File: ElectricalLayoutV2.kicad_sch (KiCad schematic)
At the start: 21 parts, among them U1 DS18B20, U2 DS18B20, U3 DS18B20, U4 DS18B20

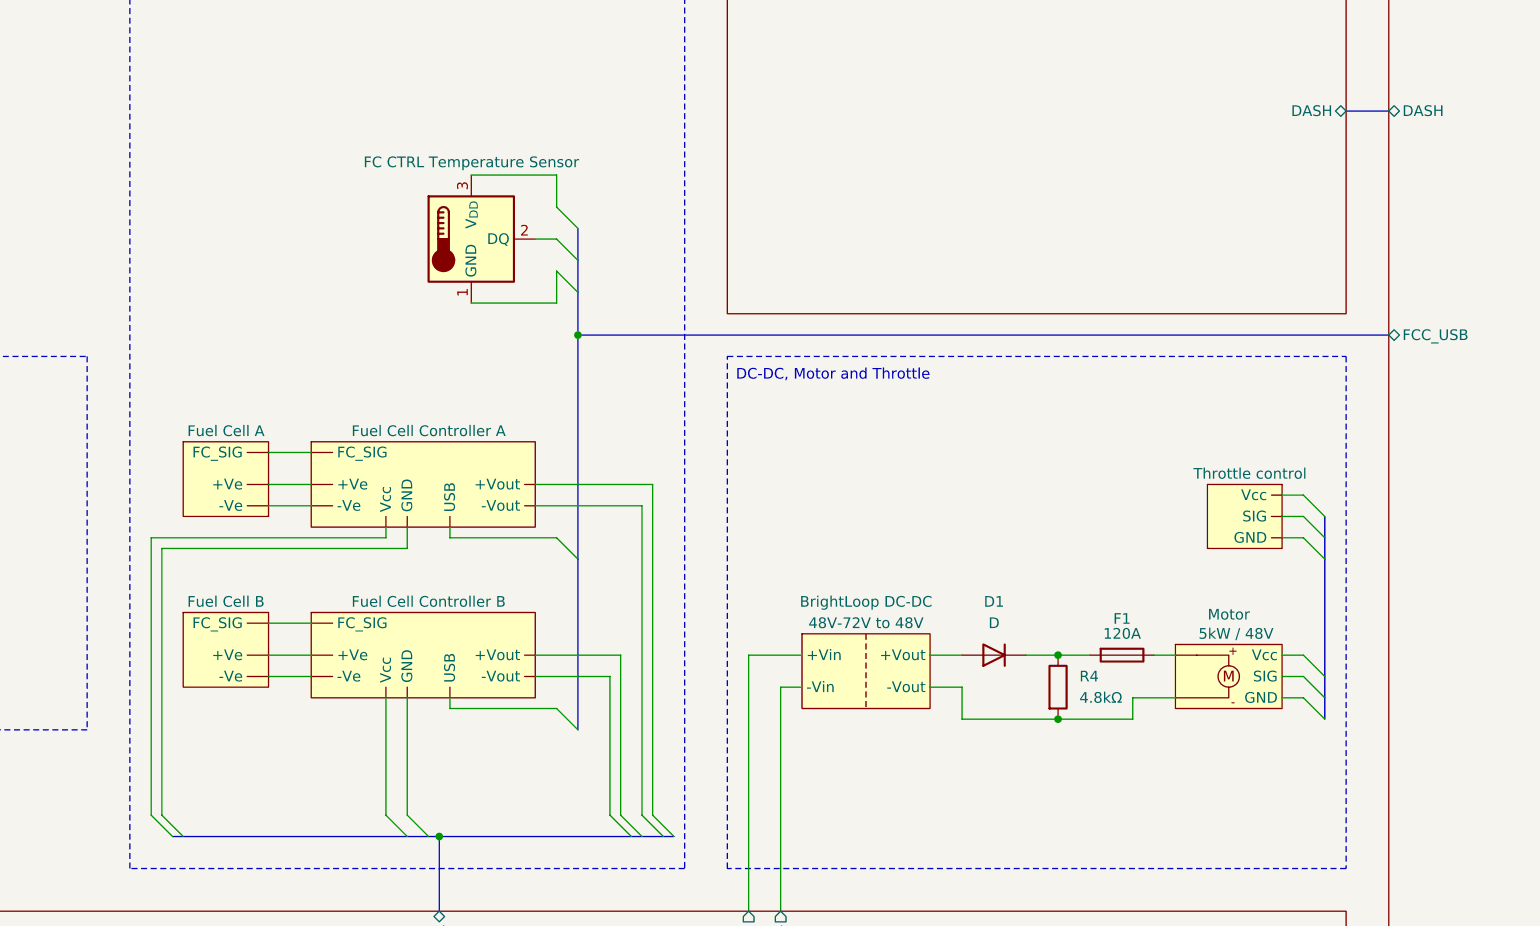
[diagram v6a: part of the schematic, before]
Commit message: Add labels
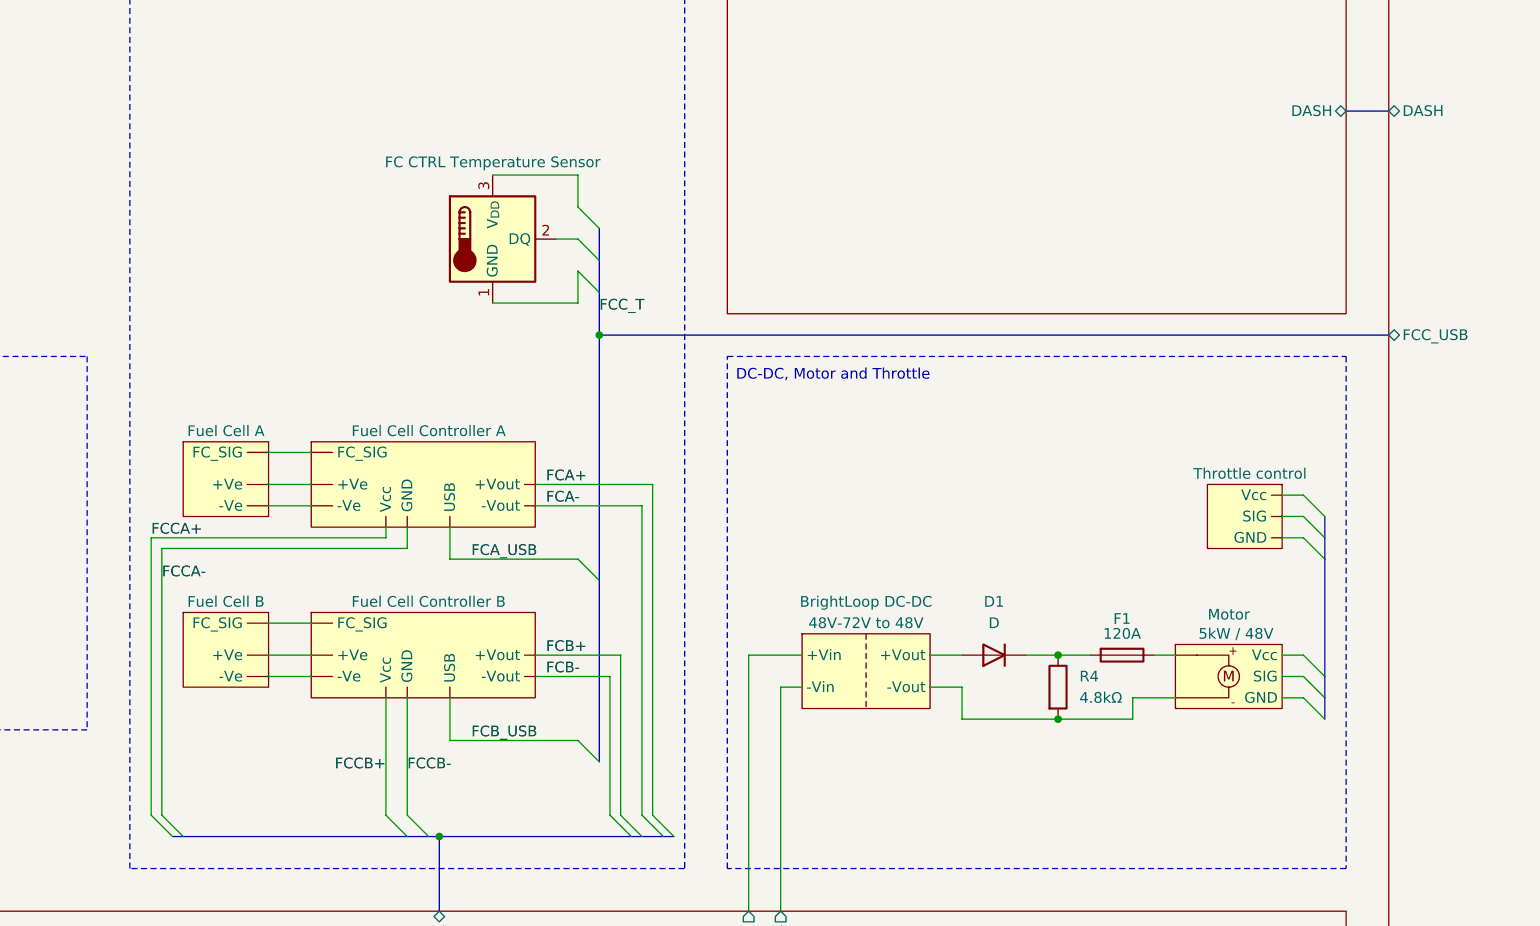
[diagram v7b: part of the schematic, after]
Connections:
- net FCCA-: now reaches FCC1. (Vcc)
- net FCCA-: no longer FC1. (FC_SIG)
- net at PROP1. (Vcc): now also DCC1. (-Vout), R4.2
- net FCCB-: now reaches FCC2. (Vcc)
- new net: FC1. (FC_SIG), FCC1. (Vcc) (x2)
- new net: FC2. (FC_SIG), FCC2. (Vcc) (x2)
- new net FCA+: FCC1. (Vcc)
- new net FCA-: FCC1. (Vcc)
- new net FCA_USB: FCC1. (Vcc)
- new net FCB+: FCC2. (Vcc)
- new net FCB-: FCC2. (Vcc)
- new net FCB_USB: FCC2. (Vcc)
- new net FCCA+: FCC1. (Vcc)
- new net FCCB+: FCC2. (Vcc)
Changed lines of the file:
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@@
 	(title_block
 		(title "Electrical Layout 2024")
-		(date "2024-06-04")
-		(rev "1.3.0")
+		(date "2024-06-13")
+		(rev "1.3.1")
 		(company "Exocet Polytechnique Montréal")
 	)
@@
 	)
 	(junction
+		(at 118.11 60.96)
+		(diameter 0)
+		(color 0 0 132 1)
+	)
+	(junction
 		(at 172.72 99.06)
 		(diameter 0)
@@
 	)
 	(junction
-		(at 115.57 60.96)
-		(diameter 0)
-		(color 0 0 0 0)
-	)
-	(junction
 		(at 172.72 106.68)
 		(diameter 0)
@@
 	)
 	(bus_entry
-		(at 113.03 105.41)
+		(at 115.57 109.22)
 		(size 2.54 2.54)
 		(stroke
@@
 	)
 	(bus_entry
-		(at 113.03 53.34)
+		(at 115.57 53.34)
 		(size 2.54 2.54)
 		(stroke
@@
 	)
 	(bus_entry
-		(at 113.03 45.72)
-		(size 2.54 2.54)
-		(stroke
-			(width 0)
-			(type default)
-		)
-	)
-	(bus_entry
-		(at 113.03 49.53)
+		(at 115.57 45.72)
+		(size 2.54 2.54)
+		(stroke
+			(width 0)
+			(type default)
+		)
+	)
+	(bus_entry
+		(at 115.57 49.53)
 		(size 2.54 2.54)
 		(stroke
@@
 	)
 	(bus_entry
-		(at 113.03 85.09)
+		(at 115.57 87.63)
 		(size 2.54 2.54)
 		(stroke
@@
 	(wire
 		(pts
-			(xy 102.87 41.91) (xy 113.03 41.91)
+			(xy 105.41 41.91) (xy 115.57 41.91)
 		)
 		(stroke
@@
 	(wire
 		(pts
-			(xy 113.03 41.91) (xy 113.03 45.72)
+			(xy 115.57 41.91) (xy 115.57 45.72)
 		)
 		(stroke
@@
 	(wire
 		(pts
-			(xy 100.33 83.82) (xy 100.33 85.09)
+			(xy 100.33 83.82) (xy 100.33 87.63)
 		)
 		(stroke
@@
 	(bus
 		(pts
-			(xy 115.57 87.63) (xy 115.57 107.95)
+			(xy 118.11 90.17) (xy 118.11 111.76)
 		)
 		(stroke
@@
 	(wire
 		(pts
-			(xy 113.03 57.15) (xy 113.03 53.34)
+			(xy 115.57 57.15) (xy 115.57 53.34)
 		)
 		(stroke
@@
 	(bus
 		(pts
-			(xy 115.57 55.88) (xy 115.57 60.96)
-		)
-		(stroke
-			(width 0)
-			(type default)
+			(xy 118.11 55.88) (xy 118.11 60.96)
+		)
+		(stroke
+			(width 0)
+			(type default)
+			(color 132 0 0 1)
 		)
 	)
@@
 	(wire
 		(pts
-			(xy 100.33 105.41) (xy 113.03 105.41)
+			(xy 100.33 109.22) (xy 115.57 109.22)
 		)
 		(stroke
@@
 		)
 	)
-	(bus
-		(pts
-			(xy 115.57 60.96) (xy 212.09 60.96)
-		)
-		(stroke
-			(width 0)
-			(type default)
-		)
-	)
 	(wire
 		(pts
@@
 	(wire
 		(pts
-			(xy 102.87 57.15) (xy 113.03 57.15)
-		)
-		(stroke
-			(width 0)
-			(type default)
-		)
-	)
-	(wire
-		(pts
-			(xy 100.33 85.09) (xy 113.03 85.09)
+			(xy 105.41 57.15) (xy 115.57 57.15)
+		)
+		(stroke
+			(width 0)
+			(type default)
+		)
+	)
+	(wire
+		(pts
+			(xy 100.33 87.63) (xy 115.57 87.63)
 		)
 		(stroke
@@
 	(bus
 		(pts
-			(xy 115.57 87.63) (xy 115.57 60.96)
+			(xy 118.11 90.17) (xy 118.11 60.96)
 		)
 		(stroke
@@
 	(bus
 		(pts
-			(xy 115.57 48.26) (xy 115.57 52.07)
-		)
-		(stroke
-			(width 0)
-			(type default)
+			(xy 118.11 48.26) (xy 118.11 52.07)
+		)
+		(stroke
+			(width 0)
+			(type default)
+			(color 132 0 0 1)
 		)
 	)
@@
 		)
 	)
+	(bus
+		(pts
+			(xy 118.11 60.96) (xy 212.09 60.96)
+		)
+		(stroke
+			(width 0)
+			(type default)
+		)
+	)
 	(wire
 		(pts
@@
 	(wire
 		(pts
-			(xy 110.49 49.53) (xy 113.03 49.53)
+			(xy 113.03 49.53) (xy 115.57 49.53)
 		)
 		(stroke
@@
 	(bus
 		(pts
-			(xy 115.57 52.07) (xy 115.57 55.88)
-		)
-		(stroke
-			(width 0)
-			(type default)
+			(xy 118.11 52.07) (xy 118.11 55.88)
+		)
+		(stroke
+			(width 0)
+			(type default)
+			(color 132 0 0 1)
 		)
 	)
@@
 	(wire
 		(pts
-			(xy 100.33 105.41) (xy 100.33 104.14)
+			(xy 100.33 109.22) (xy 100.33 104.14)
 		)
 		(stroke
@@
 				(size 1.27 1.27)
 				(color 0 0 194 1)
+			)
+			(justify left bottom)
+		)
+	)
+	(label "FCB-"
+		(at 111.76 101.6 0)
+		(fields_autoplaced yes)
+		(effects
+			(font
+				(size 1.27 1.27)
+			)
+			(justify left bottom)
+		)
+	)
+	(label "FCB+"
+		(at 111.76 99.06 0)
+		(fields_autoplaced yes)
+		(effects
+			(font
+				(size 1.27 1.27)
+			)
+			(justify left bottom)
+		)
+	)
+	(label "FCCB-"
+		(at 95.25 113.03 0)
+		(fields_autoplaced yes)
+		(effects
+			(font
+				(size 1.27 1.27)
+			)
+			(justify left bottom)
+		)
+	)
+	(label "FCCA-"
+		(at 66.04 90.17 0)
+		(fields_autoplaced yes)
+		(effects
+			(font
+				(size 1.27 1.27)
+			)
+			(justify left bottom)
+		)
+	)
+	(label "FCA+"
+		(at 111.76 78.74 0)
+		(fields_autoplaced yes)
+		(effects
+			(font
+				(size 1.27 1.27)
+			)
+			(justify left bottom)
+		)
+	)
+	(label "FCCA+"
+		(at 64.77 85.09 0)
+		(fields_autoplaced yes)
+		(effects
+			(font
+				(size 1.27 1.27)
+			)
+			(justify left bottom)
+		)
+	)
+	(label "FCB_USB"
+		(at 102.87 109.22 0)
+		(fields_autoplaced yes)
+		(effects
+			(font
+				(size 1.27 1.27)
+			)
+			(justify left bottom)
+		)
+	)
+	(label "FCCB+"
+		(at 92.71 113.03 180)
+		(fields_autoplaced yes)
+		(effects
+			(font
+				(size 1.27 1.27)
+			)
+			(justify right bottom)
+		)
+	)
+	(label "FCC_T"
+		(at 118.11 58.42 0)
+		(fields_autoplaced yes)
+		(effects
+			(font
+				(size 1.27 1.27)
+			)
+			(justify left bottom)
+		)
+	)
+	(label "FCA_USB"
+		(at 102.87 87.63 0)
+		(fields_autoplaced yes)
+		(effects
+			(font
+				(size 1.27 1.27)
+			)
+			(justify left bottom)
+		)
+	)
+	(label "FCA-"
+		(at 111.76 81.28 0)
+		(fields_autoplaced yes)
+		(effects
+			(font
+				(size 1.27 1.27)
 			)
 			(justify left bottom)
@@
 	(symbol
 		(lib_id "Sensor_Temperature:DS18B20")
-		(at 102.87 49.53 0)
+		(at 105.41 49.53 0)
 		(unit 1)
 		(exclude_from_sim no)
@@
 		(dnp no)
 		(property "Reference" "U1"
-			(at 96.52 48.2599 0)
+			(at 99.06 48.2599 0)
 			(effects
 				(font
@@
 		)
 		(property "Value" "DS18B20"
-			(at 96.52 50.7999 0)
+			(at 99.06 50.7999 0)
 			(effects
 				(font
@@
 		)
 		(property "Footprint" "Package_TO_SOT_THT:TO-92_Inline"
-			(at 77.47 55.88 0)
+			(at 80.01 55.88 0)
 			(effects
 				(font
@@
 		)
 		(property "Datasheet" "http://datasheets.maximintegrated.com/en/ds/DS18B20.pdf"
-			(at 99.06 43.18 0)
+			(at 101.6 43.18 0)
 			(effects
 				(font
@@
 		)
 		(property "Description" "Programmable Resolution 1-Wire Digital Thermometer TO-92"
-			(at 102.87 49.53 0)
+			(at 105.41 49.53 0)
 			(effects
 				(font
@@
 		)
 		(property "Name" "FC CTRL Temperature Sensor"
-			(at 102.87 40.386 0)
-			(effects
-				(font
+			(at 105.41 40.386 0)
+			(effects
+				(font
